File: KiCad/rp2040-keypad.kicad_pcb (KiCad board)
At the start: 4 copper layers, 32 parts, among them J1 USB_C_Receptacle_USB2.0, J2 Conn_01x04_Male, SW1 SW_Push, SW2 SW_Push, U1 AMS1117-3.3, U2 RP2040, U3 W25Q128JVS, Y1 X322512MSB4SI

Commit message: First draft completed ready to review
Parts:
- added H1: MountingHole, MountingHole:MountingHole_2.2mm_M2_DIN965, F.Cu at (138.0, 60.0)
- added H2: MountingHole, MountingHole:MountingHole_2.2mm_M2_DIN965, F.Cu at (138.0, 102.2)
- added H3: MountingHole, MountingHole:MountingHole_2.2mm_M2_DIN965, F.Cu at (181.5, 102.2)
- added H4: MountingHole, MountingHole:MountingHole_2.2mm_M2_DIN965, F.Cu at (181.5, 60.0)
- R3, R4: value 27R -> 27R4
- Y1: value X322512MSB4SI -> 12Mhz
- moved C1 155.9 mm to (178.2, 61.6), turned to -90 degrees
- moved R6 144.4 mm to (166.6, 82.1), turned to -90 degrees
- moved C2 136.5 mm to (168.2, 61.6), turned to -90 degrees
- moved SW2 135.1 mm to (149.7, 90.9)
- moved R1 134.8 mm to (165.7, 66.3), turned to 90 degrees
- moved SW1 134.1 mm to (168.8, 90.9)
- moved R4 132.7 mm to (160.2, 68.8), turned to 90 degrees
- moved U3 124.8 mm to (147.7, 71.8)
- moved C13 123.8 mm to (164.4, 75.2)
- moved R2 122.8 mm to (153.4, 66.3), turned to 90 degrees
- moved R5 122.6 mm to (151.2, 77.2), turned to 90 degrees
- moved C15 121.2 mm to (154.4, 69.8)
- moved C17 120.9 mm to (173.9, 81.3), turned to -90 degrees
- moved J2 120.7 mm to (140.6, 64.0)
- moved Y1 120.6 mm to (171.2, 81.8), turned to 180 degrees
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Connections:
- R6 pad 1: Net-(R6-Pad1) -> Net-(C17-Pad1)
- U2 pad 20: Net-(U2-Pad20) -> Net-(C16-Pad1)
- Y1 pad 1: Net-(C16-Pad1) -> Net-(C17-Pad1)
- Y1 pad 2: Net-(U2-Pad20) -> GND
- Y1 pad 3: Net-(C17-Pad1) -> Net-(C16-Pad1)
- Y1 pad 4: Net-(R6-Pad1) -> GND
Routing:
- net +3V3: track 0.00 -> 55.8 mm, vias 0 -> 10
- net GND: track 0.00 -> 49.3 mm, vias 0 -> 38
- net /SWD: track 0.00 -> 34.7 mm, vias 0 -> 1
- net /SWCLK: track 0.00 -> 25.5 mm, vias 0 -> 1
- net +1V1: track 0.00 -> 23.4 mm, vias 0 -> 3
- net VBUS: track 0.00 -> 22.1 mm
- net /QSPI_SS: track 0.00 -> 17.1 mm, vias 0 -> 2
- net unconnected-(J1-PadS1): track 0.00 -> 17.0 mm
- net /KEY1: track 0.00 -> 17.0 mm, vias 0 -> 1
- net /QSPI_SD1: track 0.00 -> 16.5 mm, vias 0 -> 2
- net /KEY2: track 0.00 -> 15.6 mm
- net /QSPI_SD2: track 0.00 -> 15.4 mm
- net Net-(C16-Pad1): track 0.00 -> 13.9 mm
- net Net-(R6-Pad2): track 0.00 -> 9.53 mm
- net Net-(C17-Pad1): track 0.00 -> 9.26 mm
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- added copper zone on In2.Cu, net +3V3
- added copper zone on In1.Cu, net GND
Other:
- board outline added: 48.1 x 46.8 mm
- board text added: "3V3"
- board text added: "GND"
- board text added: "RP2040-Keypad"
- board text added: "SWCK"
- board text added: "SWD"
- board text added: "https://github.com/adrianuseb/rp2040-keypad"

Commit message: Rev 0.1 ready for production
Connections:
- net Net-(R3-Pad2) renamed /D+
- net Net-(R4-Pad1) renamed /D-
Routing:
- net /USB_D+: track 4.23 -> 5.84 mm
- added copper zone on F.Cu, net +3V3
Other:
- board text added: "Rev 0.1"
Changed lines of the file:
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@@
   (net 15 "/SWCLK")
   (net 16 "/NUSB_BOOT")
-  (net 17 "Net-(R3-Pad2)")
-  (net 18 "Net-(R4-Pad1)")
+  (net 17 "/D+")
+  (net 18 "/D-")
   (net 19 "/QSPI_SS")
   (net 20 "Net-(R6-Pad2)")
@@
     (fp_line (start -0.525 -0.27) (end 0.525 -0.27) (layer "F.Fab") (width 0.1))
     (pad "1" smd roundrect (at -0.51 0 90) (size 0.54 0.64) (layers "F.Cu" "F.Paste" "F.Mask") (roundrect_rratio 0.25)
-      (net 18 "Net-(R4-Pad1)") (pintype "passive"))
+      (net 18 "/D-") (pintype "passive"))
     (pad "2" smd roundrect (at 0.51 0 90) (size 0.54 0.64) (layers "F.Cu" "F.Paste" "F.Mask") (roundrect_rratio 0.25)
       (net 9 "/USB_D-") (pintype "passive"))
@@
       (net 4 "+1V1") (pinfunction "VREG_VOUT") (pintype "power_out"))
     (pad "46" smd roundrect locked (at 1.4 -3.4375) (size 0.2 0.875) (layers "F.Cu" "F.Paste" "F.Mask") (roundrect_rratio 0.25)
-      (net 18 "Net-(R4-Pad1)") (pinfunction "USB_DM") (pintype "bidirectional"))
+      (net 18 "/D-") (pinfunction "USB_DM") (pintype "bidirectional"))
     (pad "47" smd roundrect locked (at 1 -3.4375) (size 0.2 0.875) (layers "F.Cu" "F.Paste" "F.Mask") (roundrect_rratio 0.25)
-      (net 17 "Net-(R3-Pad2)") (pinfunction "USB_DP") (pintype "bidirectional"))
+      (net 17 "/D+") (pinfunction "USB_DP") (pintype "bidirectional"))
     (pad "48" smd roundrect locked (at 0.6 -3.4375) (size 0.2 0.875) (layers "F.Cu" "F.Paste" "F.Mask") (roundrect_rratio 0.25)
       (net 1 "+3V3") (pinfunction "USB_VDD") (pintype "power_in"))
@@
       (net 8 "/USB_D+") (pintype "passive"))
     (pad "2" smd roundrect (at 0.51 0 270) (size 0.54 0.64) (layers "F.Cu" "F.Paste" "F.Mask") (roundrect_rratio 0.25)
-      (net 17 "Net-(R3-Pad2)") (pintype "passive"))
+      (net 17 "/D+") (pintype "passive"))
     (model "${KICAD6_3DMODEL_DIR}/Resistor_SMD.3dshapes/R_0402_1005Metric.wrl"
       (offset (xyz 0 0 0))
@@
   (gr_arc (start 138 104.525) (mid 136.373654 103.851346) (end 135.7 102.225) (layer "Edge.Cuts") (width 0.1))
   (gr_arc (start 135.7 60.05) (mid 136.373654 58.423654) (end 138 57.75) (layer "Edge.Cuts") (width 0.1))
+  (gr_text "Rev 0.1" (at 181.5 97.725) (layer "F.SilkS")
+    (effects (font (size 0.5 0.5) (thickness 0.1)))
+  )
   (gr_text "GND" (at 151.4 62.2) (layer "F.SilkS")
     (effects (font (size 0.5 0.5) (thickness 0.1)))
@@
   (segment (start 165.7 67.3) (end 165.7 66.835) (width 0.3) (layer "F.Cu") (net 7))
   (segment (start 160.75 67.12) (end 161.43 67.8) (width 0.3) (layer "F.Cu") (net 7))
-  (segment (start 159.05 68.29) (end 159.05 67.35) (width 0.2) (layer "F.Cu") (net 8))
   (segment (start 159.75 67.05) (end 159.5 67.3) (width 0.3) (layer "F.Cu") (net 8))
   (segment (start 158.75 67.05) (end 158.75 66.045) (width 0.3) (layer "F.Cu") (net 8))
+  (segment (start 159.75 66.045) (end 159.75 67.132501) (width 0.2) (layer "F.Cu") (net 8))
+  (segment (start 159.775 67.157501) (end 159.775 67.565) (width 0.2) (layer "F.Cu") (net 8))
   (segment (start 159.5 67.3) (end 159 67.3) (width 0.3) (layer "F.Cu") (net 8))
   (segment (start 159 67.3) (end 158.75 67.05) (width 0.3) (layer "F.Cu") (net 8))
+  (segment (start 159.775 67.565) (end 159.05 68.29) (width 0.2) (layer "F.Cu") (net 8))
+  (segment (start 159.75 67.132501) (end 159.775 67.157501) (width 0.2) (layer "F.Cu") (net 8))
   (segment (start 159.05 67.35) (end 159 67.3) (width 0.2) (layer "F.Cu") (net 8))
   (segment (start 159.75 66.045) (end 159.75 67.05) (width 0.3) (layer "F.Cu") (net 8))
   (segment (start 159.98 64.7) (end 160.25 64.97) (width 0.3) (layer "F.Cu") (net 9))
+  (segment (start 160.25 66.045) (end 160.25 67.132501) (width 0.2) (layer "F.Cu") (net 9))
   (segment (start 159.57 64.7) (end 159.98 64.7) (width 0.3) (layer "F.Cu") (net 9))
-  (segment (start 160.25 68.29) (end 160.25 66.045) (width 0.2) (layer "F.Cu") (net 9))
+  (segment (start 160.25 67.132501) (end 160.225 67.157501) (width 0.2) (layer "F.Cu") (net 9))
+  (segment (start 160.225 68.265) (end 160.25 68.29) (width 0.2) (layer "F.Cu") (net 9))
   (segment (start 160.25 64.97) (end 160.25 66.045) (width 0.3) (layer "F.Cu") (net 9))
   (segment (start 159.25 66.045) (end 159.25 65.02) (width 0.3) (layer "F.Cu") (net 9))
   (segment (start 159.25 65.02) (end 159.57 64.7) (width 0.3) (layer "F.Cu") (net 9))
+  (segment (start 160.225 67.157501) (end 160.225 68.265) (width 0.2) (layer "F.Cu") (net 9))
   (segment (start 157.75 66.045) (end 157.75 67.25) (width 0.3) (layer "F.Cu") (net 11))
   (segment (start 154 67.8) (end 153.4 67.2) (width 0.3) (layer "F.Cu") (net 11))
@@
   (segment (start 151.2 77.7) (end 151.025 77.525) (width 0.2) (layer "F.Cu") (net 16))
   (segment (start 151.025 77.525) (end 148.15 77.525) (width 0.2) (layer "F.Cu") (net 16))
-  (segment (start 159.95 71.315686) (end 159.8 71.165685) (width 0.2) (layer "F.Cu") (net 17))
-  (segment (start 159.8 71.165685) (end 159.8 70.06) (width 0.2) (layer "F.Cu") (net 17))
-  (segment (start 159.8 70.06) (end 159.05 69.31) (width 0.2) (layer "F.Cu") (net 17))
-  (segment (start 159.95 74.3625) (end 159.95 71.315686) (width 0.2) (layer "F.Cu") (net 17))
-  (segment (start 160.35 74.3625) (end 160.35 71.15) (width 0.2) (layer "F.Cu") (net 18))
-  (segment (start 160.35 71.15) (end 160.2 71) (width 0.2) (layer "F.Cu") (net 18))
-  (segment (start 160.2 71) (end 160.2 69.36) (width 0.2) (layer "F.Cu") (net 18))
+  (segment (start 159.55 72.984314) (end 159.95 73.384315) (width 0.2) (layer "F.Cu") (net 17))
+  (segment (start 159.424999 72.139313) (end 159.55 72.264315) (width 0.2) (layer "F.Cu") (net 17))
+  (segment (start 159.55 72.264315) (end 159.55 72.984314) (width 0.2) (layer "F.Cu") (net 17))
+  (segment (start 159.05 69.31) (end 159.424999 69.684999) (width 0.2) (layer "F.Cu") (net 17))
+  (segment (start 159.424999 69.684999) (end 159.424999 72.139313) (width 0.2) (layer "F.Cu") (net 17))
+  (segment (start 159.95 73.384315) (end 159.95 74.025) (width 0.2) (layer "F.Cu") (net 17))
+  (segment (start 159.999982 72.077929) (end 159.999981 72.868611) (width 0.2) (layer "F.Cu") (net 18))
+  (segment (start 160.35 73.21863) (end 160.35 74.3625) (width 0.2) (layer "F.Cu") (net 18))
+  (segment (start 160.25 69.31) (end 159.875001 69.684999) (width 0.2) (layer "F.Cu") (net 18))
+  (segment (start 159.999981 72.868611) (end 160.35 73.21863) (width 0.2) (layer "F.Cu") (net 18))
   (segment (start 160.2 69.36) (end 160.25 69.31) (width 0.2) (layer "F.Cu") (net 18))
+  (segment (start 159.875001 69.684999) (end 159.875001 71.952947) (width 0.2) (layer "F.Cu") (net 18))
+  (segment (start 159.875001 71.952947) (end 159.999982 72.077929) (width 0.2) (layer "F.Cu") (net 18))
   (segment (start 145.245 69.845) (end 144.05 69.845) (width 0.2) (layer "F.Cu") (net 19))
   (segment (start 156.35 74.3625) (end 153.0375 74.3625) (width 0.2) (layer "F.Cu") (net 19))
@@
   (segment (start 157.4 75.4) (end 157.172182 75.172182) (width 0.2) (layer "B.Cu") (net 56))
   (segment (start 156.995027 75.172182) (end 153.022845 71.2) (width 0.2) (layer "B.Cu") (net 56))
+  (zone (net 1) (net_name "+3V3") (layer "F.Cu") (hatch edge 0.508)
+    (connect_pads (clearance 0.508))
+    (min_thickness 0.254) (filled_areas_thickness no)
+    (fill yes (thermal_gap 0.508) (thermal_bridge_width 0.508))
+    (polygon
+      (pts
+        (xy 177 70.025)
+        (xy 169.5 70.025)
+        (xy 169.5 63.625)
+        (xy 176.9 63.625)
+      )
+    )
+  )
   (zone (net 2) (net_name "GND") (layer "In1.Cu") (hatch edge 0.508)
     (connect_pads (clearance 0.508))

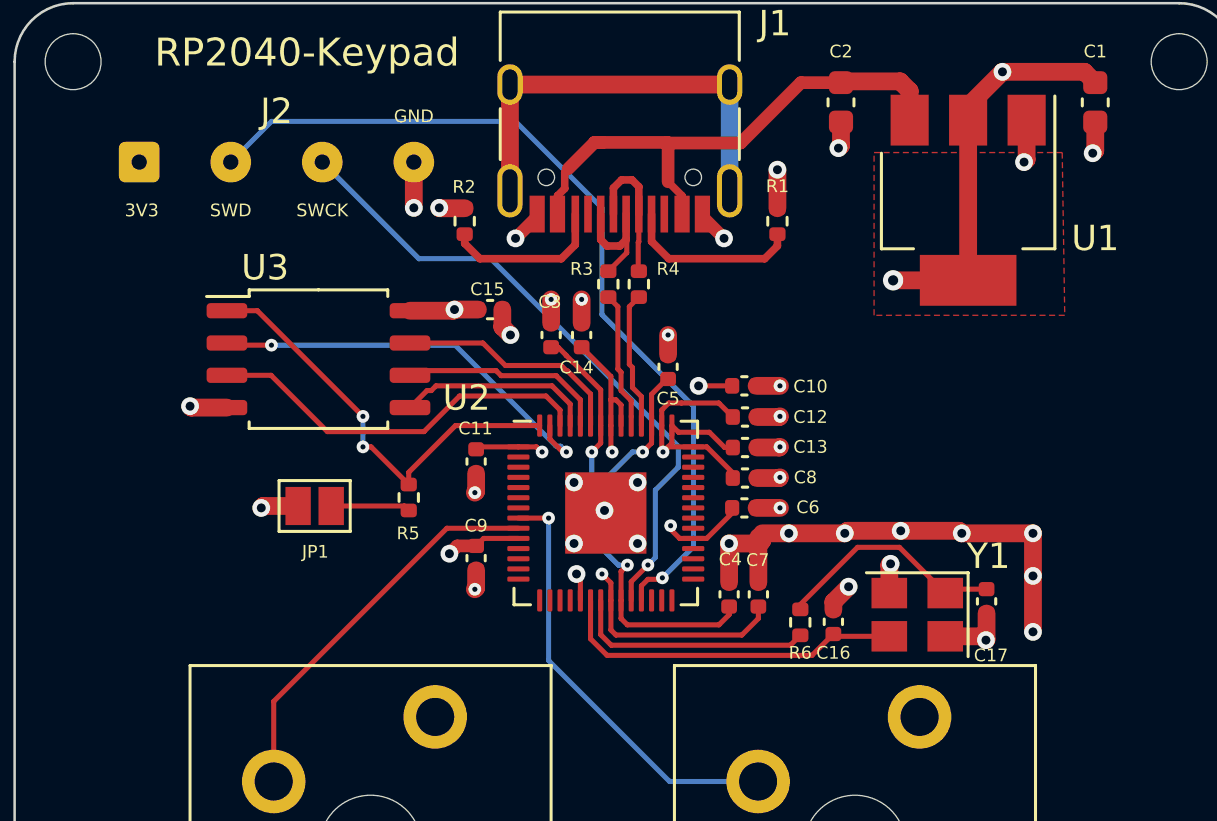
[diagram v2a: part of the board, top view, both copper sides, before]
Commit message: Update silkscreen position and information
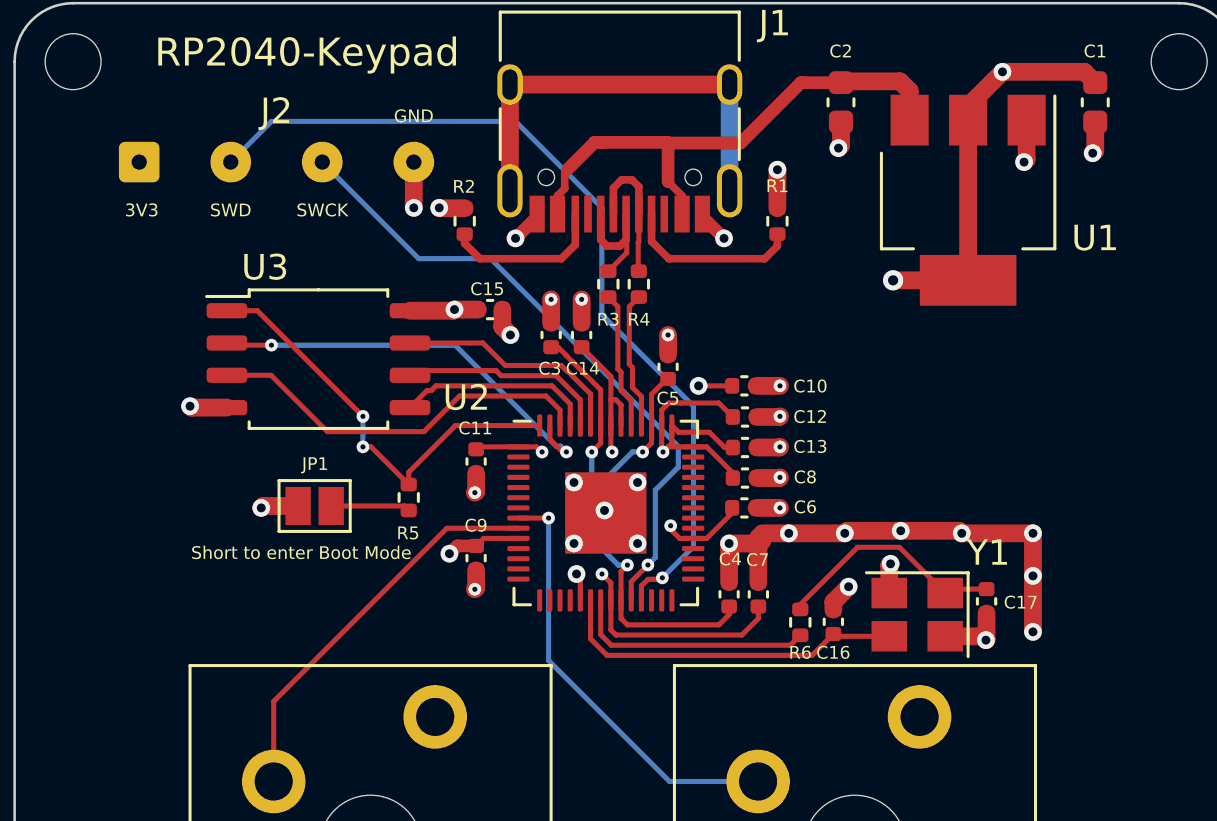
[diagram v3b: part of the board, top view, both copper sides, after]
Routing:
- removed copper zone on F.Cu, net +3V3
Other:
- board text added: "Short to enter Boot Mode"
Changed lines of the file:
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@@
     (property "Sheetname" "")
     (attr smd)
-    (fp_text reference "C6" (at 2.5 -0.025) (layer "F.SilkS")
+    (fp_text reference "C6" (at 2.4 -0.025) (layer "F.SilkS")
       (effects (font (size 0.5 0.5) (thickness 0.1)))
     )
@@
     (property "Sheetname" "")
     (attr smd)
-    (fp_text reference "Y1" (at -2.8 2.3) (layer "F.SilkS")
+    (fp_text reference "Y1" (at -2.8 2.425) (layer "F.SilkS")
       (effects (font (size 1 1) (thickness 0.15)))
     )
@@
     (property "Sheetname" "")
     (attr smd)
-    (fp_text reference "R4" (at 0.6 1.15 180) (layer "F.SilkS")
+    (fp_text reference "R4" (at -1.4 0 180) (layer "F.SilkS")
       (effects (font (size 0.5 0.5) (thickness 0.1)))
     )
@@
     (property "Sheetname" "")
     (attr smd)
-    (fp_text reference "C14" (at -1.275 -0.2 180) (layer "F.SilkS")
+    (fp_text reference "C14" (at -1.325 0.05 180) (layer "F.SilkS")
       (effects (font (size 0.5 0.5) (thickness 0.1)))
     )
@@
     (property "Sheetname" "")
     (attr smd)
-    (fp_text reference "C17" (at 2.125 -0.175 180) (layer "F.SilkS")
+    (fp_text reference "C17" (at 0.05 -1.35 180) (layer "F.SilkS")
       (effects (font (size 0.5 0.5) (thickness 0.1)))
     )
@@
     (property "Sheetname" "")
     (attr exclude_from_pos_files)
-    (fp_text reference "JP1" (at 0.025 1.8) (layer "F.SilkS")
+    (fp_text reference "JP1" (at 0.025 -1.65) (layer "F.SilkS")
       (effects (font (size 0.5 0.5) (thickness 0.1)))
     )
@@
     (property "Sheetname" "")
     (attr smd)
-    (fp_text reference "C3" (at 1.3 -0.05 180) (layer "F.SilkS")
+    (fp_text reference "C3" (at -1.325 -0.05 180) (layer "F.SilkS")
       (effects (font (size 0.5 0.5) (thickness 0.1)))
     )
@@
     (property "Sheetname" "")
     (attr smd)
-    (fp_text reference "R3" (at -0.6 1.05 180) (layer "F.SilkS")
+    (fp_text reference "R3" (at 1.4 0 180) (layer "F.SilkS")
       (effects (font (size 0.5 0.5) (thickness 0.1)))
     )
@@
   (gr_arc (start 138 104.525) (mid 136.373654 103.851346) (end 135.7 102.225) (layer "Edge.Cuts") (width 0.1))
   (gr_arc (start 135.7 60.05) (mid 136.373654 58.423654) (end 138 57.75) (layer "Edge.Cuts") (width 0.1))
+  (gr_text "GND" (at 151.4 62.2) (layer "B.SilkS")
+    (effects (font (size 0.5 0.5) (thickness 0.1)))
+  )
+  (gr_text "3V3" (at 140.575 62.2) (layer "B.SilkS")
+    (effects (font (size 0.5 0.5) (thickness 0.1)))
+  )
+  (gr_text "SWCK" (at 147.975 62.15) (layer "B.SilkS")
+    (effects (font (size 0.5 0.5) (thickness 0.1)))
+  )
+  (gr_text "SWD" (at 144.25 62.15) (layer "B.SilkS")
+    (effects (font (size 0.5 0.5) (thickness 0.1)))
+  )
   (gr_text "Rev 0.1" (at 181.5 97.725) (layer "F.SilkS")
     (effects (font (size 0.5 0.5) (thickness 0.1)))
@@
   )
   (gr_text "SWD" (at 144.2 65.9) (layer "F.SilkS")
+    (effects (font (size 0.5 0.5) (thickness 0.1)))
+  )
+  (gr_text "Short to enter Boot Mode" (at 146.975 79.375) (layer "F.SilkS")
     (effects (font (size 0.5 0.5) (thickness 0.1)))
   )
@@
   (segment (start 157.4 75.4) (end 157.172182 75.172182) (width 0.2) (layer "B.Cu") (net 56))
   (segment (start 156.995027 75.172182) (end 153.022845 71.2) (width 0.2) (layer "B.Cu") (net 56))
-  (zone (net 1) (net_name "+3V3") (layer "F.Cu") (hatch edge 0.508)
-    (connect_pads (clearance 0.508))
-    (min_thickness 0.254) (filled_areas_thickness no)
-    (fill yes (thermal_gap 0.508) (thermal_bridge_width 0.508))
-    (polygon
-      (pts
-        (xy 177 70.025)
-        (xy 169.5 70.025)
-        (xy 169.5 63.625)
-        (xy 176.9 63.625)
-      )
-    )
-  )
   (zone (net 2) (net_name "GND") (layer "In1.Cu") (hatch edge 0.508)
     (connect_pads (clearance 0.508))
